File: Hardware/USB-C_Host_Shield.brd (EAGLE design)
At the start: 53.3 x 59.7 mm, 74 parts, among them J1 USB-C, J2 GPIN, J3 GPOUT, U1 ARDUINO_UNO_R3_SHIELDBASIC, U2 LM1117, U3 74HC4050, U5 MAX3421, U6 3.3V/150mA, Y1 12.0mhZ

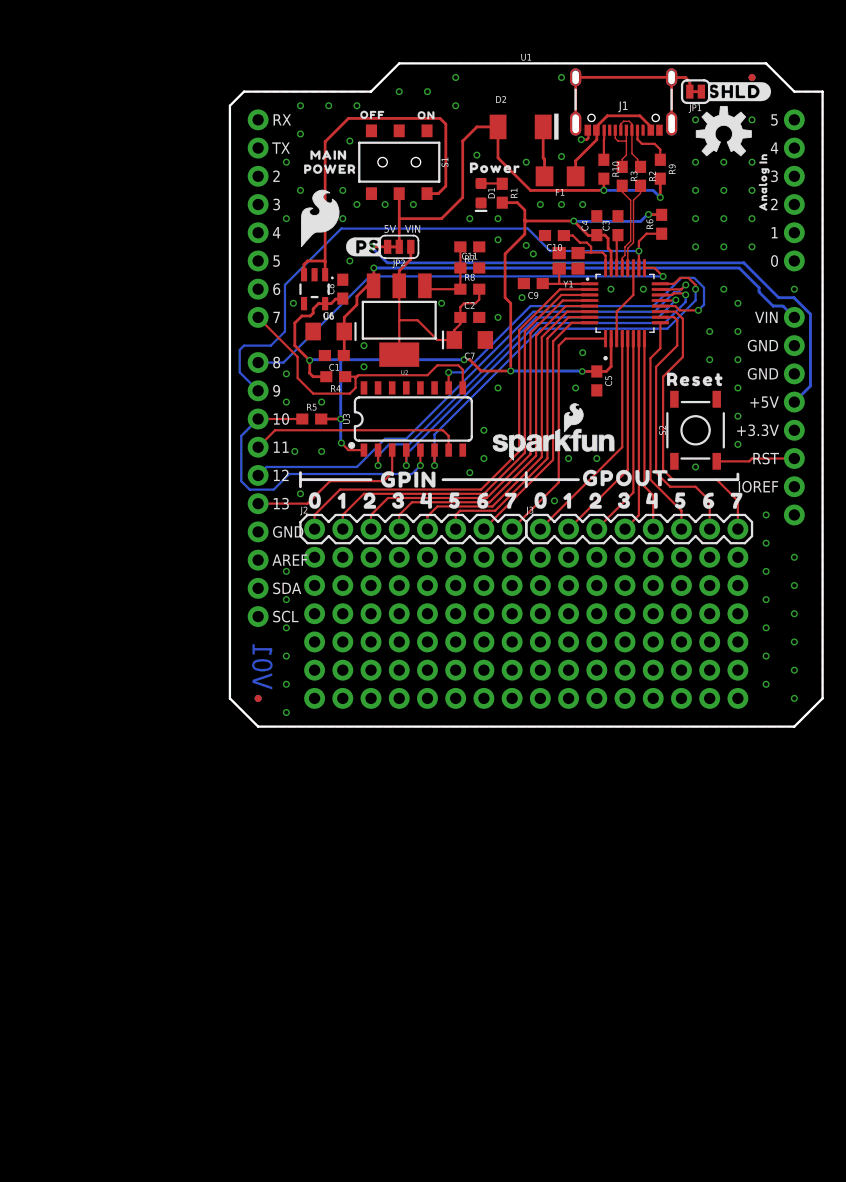
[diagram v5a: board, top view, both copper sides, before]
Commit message: Finalized schematic
Added new switch instead of trace jumper for power switch between VIN and 5V
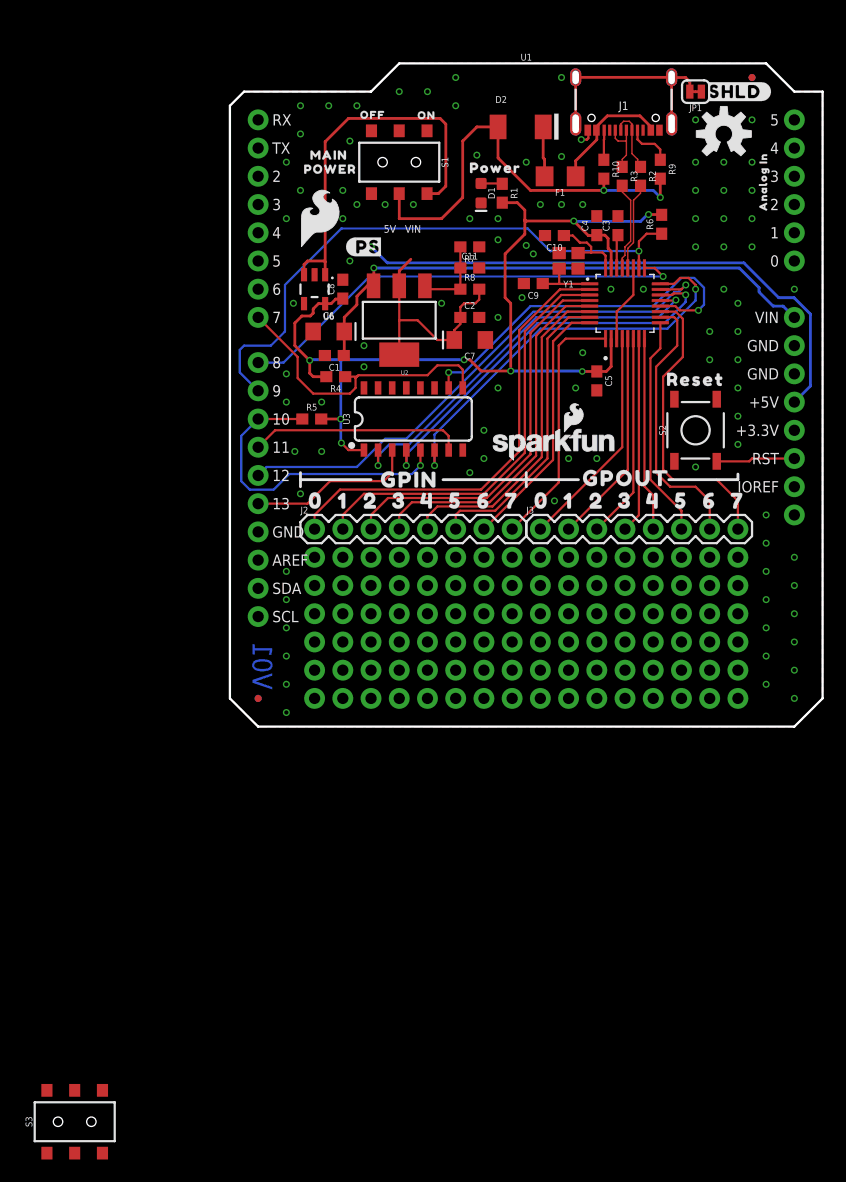
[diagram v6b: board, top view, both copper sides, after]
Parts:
- removed JP2: Power Select, SparkFun-Jumpers:SMT-JUMPER_3_1-NC_TRACE_SILK
- added S3: Power Select, SparkFun-Switches:SWITCH_DPDT_SMD_AYZ0202
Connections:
- net 5V: now also S3.3; no longer JP2.3
- net N$6: now also S3.1; no longer JP2.1
- net VDD: now also S3.2; no longer JP2.2
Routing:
- net VDD: track 41.7 -> 39.2 mm
- net 5V: track 52.0 -> 50.5 mm
- net N$6: track 21.9 -> 20.8 mm
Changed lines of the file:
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@@
 <layer number="44" name="Drills" color="7" fill="1" visible="no" active="yes"/>
 <layer number="45" name="Holes" color="7" fill="1" visible="yes" active="yes"/>
-<layer number="46" name="Milling" color="3" fill="1" visible="yes" active="yes"/>
+<layer number="46" name="Milling" color="3" fill="1" visible="no" active="yes"/>
 <layer number="47" name="Measures" color="7" fill="1" visible="no" active="yes"/>
 <layer number="48" name="Document" color="7" fill="1" visible="no" active="yes"/>
@@
 <attribute name="VALUE" x="9.525" y="29.718" size="0.6096" layer="27" font="vector" ratio="20" rot="R180" align="top-center"/>
 </element>
-<element name="JP2" library="SparkFun-Jumpers" package="SMT-JUMPER_3_1-NC_TRACE_SILK" package3d_urn="urn:adsk.eagle:package:39288/1" value="Power Select" x="15.24" y="40.64" smashed="yes" rot="R180">
-<attribute name="NAME" x="15.24" y="39.497" size="0.6096" layer="25" font="vector" ratio="20" rot="R180" align="bottom-center"/>
-<attribute name="VALUE" x="15.24" y="41.783" size="0.6096" layer="27" font="vector" ratio="20" rot="R180" align="top-center"/>
-</element>
 <element name="U$10" library="output" package="#PS7654332156" value="" x="12.446" y="40.64" smashed="yes"/>
 <element name="R5" library="SparkFun-Resistors" package="0603" value="2.2k" x="7.366" y="25.146" smashed="yes">
@@
 <element name="U5" library="SparkFun-IC-Microcontroller" package="TQFP32" value="MAX3421" x="35.56" y="35.56" smashed="yes" rot="R90">
 <attribute name="PROD_ID" value="IC-09517" x="35.56" y="35.56" size="1.778" layer="27" font="vector" ratio="15" rot="R90" display="off"/>
+</element>
+<element name="S3" library="SparkFun-Switches" package="SWITCH_DPDT_SMD_AYZ0202" value="Power Select" x="-13.97" y="-38.1" smashed="yes">
+<attribute name="NAME" x="-17.78" y="-38.1" size="0.6096" layer="25" font="vector" ratio="20" rot="R90" align="bottom-center"/>
+<attribute name="PROD_ID" value="SWCH-08179" x="-13.97" y="-38.1" size="1.778" layer="27" font="vector" ratio="15" display="off"/>
+<attribute name="SF_ID" value="COM-00597" x="-13.97" y="-38.1" size="1.778" layer="27" font="vector" ratio="15" display="off"/>
+<attribute name="VALUE" x="-10.16" y="-38.1" size="0.6096" layer="27" font="vector" ratio="20" rot="R90" align="top-center"/>
 </element>
 </elements>
@@
 <wire x1="52.25" y1="34.583" x2="52.25" y2="28.12" width="0.254" layer="16"/>
 <wire x1="52.25" y1="28.12" x2="50.8" y2="26.67" width="0.254" layer="16"/>
-<contactref element="JP2" pad="3"/>
 <via x="12.725" y="40.64" extent="1-16" drill="0.381"/>
-<wire x1="12.725" y1="40.64" x2="14.1986" y2="40.64" width="0.254" layer="1"/>
+<contactref element="S3" pad="3"/>
+<wire x1="-11.47" y1="-35.275" x2="12.725" y2="40.64" width="0" layer="19" extent="1-1"/>
 </signal>
 <signal name="SCK-IN">
@@
 <wire x1="20.74" y1="33.694" x2="20.74" y2="34.29" width="0.2032" layer="1"/>
 <wire x1="20.19" y1="33.144" x2="20.74" y2="33.694" width="0.2032" layer="1"/>
-<contactref element="JP2" pad="1"/>
-<wire x1="16.2814" y1="39.5224" x2="16.2814" y2="40.64" width="0.254" layer="1"/>
 <wire x1="15.24" y1="38.481" x2="16.2814" y2="39.5224" width="0.254" layer="1"/>
+<contactref element="S3" pad="1"/>
+<wire x1="15.24" y1="30.937" x2="-16.47" y2="-35.275" width="0" layer="19" extent="1-1"/>
 </signal>
 <signal name="N$8">
@@
 <via x="38.735" y="45.085" extent="1-16" drill="0.381"/>
 <wire x1="38.735" y1="46.775" x2="38.735" y2="45.085" width="0.254" layer="1"/>
-<contactref element="JP2" pad="2"/>
 <contactref element="S1" pad="2"/>
-<wire x1="15.24" y1="40.64" x2="15.24" y2="43.18" width="0.254" layer="1"/>
 <wire x1="15.24" y1="43.18" x2="15.24" y2="45.435" width="0.254" layer="1"/>
 <wire x1="19.05" y1="43.18" x2="15.24" y2="43.18" width="0.254" layer="1"/>
@@
 <wire x1="33.655" y1="45.72" x2="38.1" y2="45.72" width="0.254" layer="16"/>
 <wire x1="38.1" y1="45.72" x2="38.735" y2="45.085" width="0.254" layer="16"/>
+<contactref element="S3" pad="2"/>
+<wire x1="-13.97" y1="-35.275" x2="15.24" y2="45.435" width="0" layer="19" extent="1-1"/>
 </signal>
 <signal name="N$5">

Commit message: Updated layout
Completed layout changes from adding new switch and adjusting the silk screen to be buzzard labels
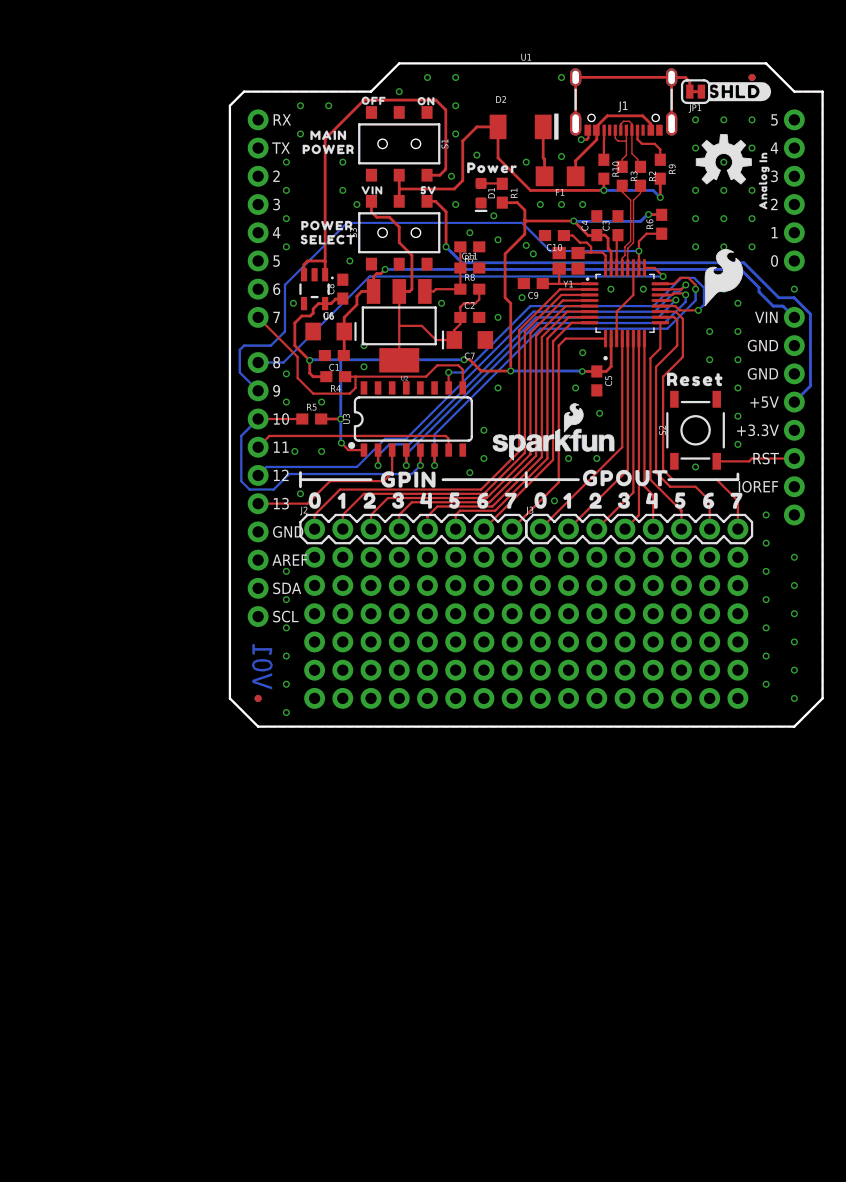
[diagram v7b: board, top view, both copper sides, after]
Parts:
- added U$1: (no value), output:5V6
- added U$12: (no value), output:VIN7
- added U$13: (no value), output:SELECT12
- U$10: device output:#PS7654332156 -> output:POWER11
- moved S3 85.2 mm to (15.2, 41.9)
- moved U$4 36.7 mm to (44.5, 37.8)
- moved U$10 4.15 mm to (8.76, 42.5)
- moved LOGO1 2.54 mm to (44.5, 48.3)
- moved U$14 1.78 mm to (8.89, 49.4)
- moved U$15 1.78 mm to (8.89, 50.7)
- moved S1 1.65 mm to (15.2, 49.9)
- moved U$7 1.28 mm to (13.0, 53.8)
- moved U$5 1.27 mm to (17.7, 53.7)
- moved U2 0.51 mm to (15.2, 33.5)
- moved U$2 0.25 mm to (23.6, 47.8)
- moved U$8 0.13 mm to (48.0, 46.6)
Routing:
- net N$6: track 20.8 -> 29.1 mm
- net VDD: track 39.2 -> 37.3 mm
- net 5V: track 50.5 -> 49.1 mm
- net POWER_IN: track 34.4 -> 35.1 mm
- net PICO: track 19.3 -> 18.7 mm
- net GND: track 8.71 -> 8.41 mm, vias 98 -> 100
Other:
- board text removed: "5V"
- board text removed: "VIN"

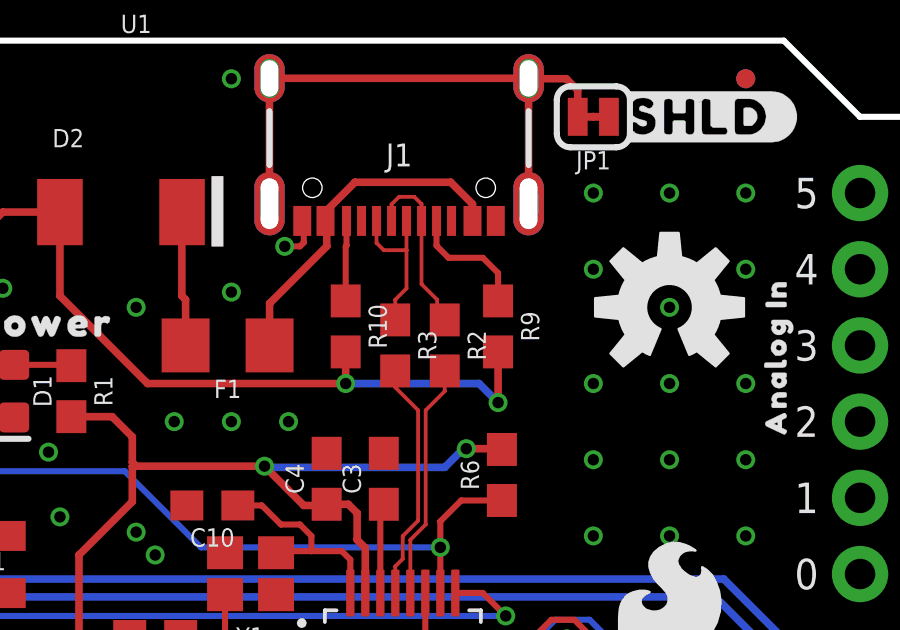
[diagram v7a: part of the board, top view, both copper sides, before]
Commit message: Added product ID to R9 and R10
Created new part in Sparkle for this 56k 0603 resistor that is already input. The new ID, RES-17211, was added to the part and going to be add to the SparkFun parts library after project is verified with components and all
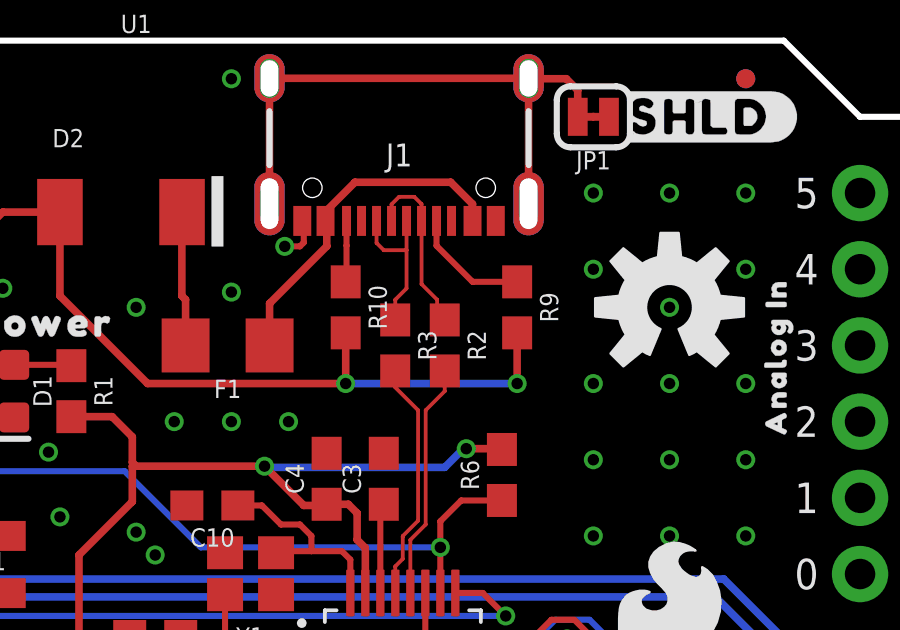
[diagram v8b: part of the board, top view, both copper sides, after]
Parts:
- moved R9 0.90 mm to (39.4, 48.3)
- moved R10 0.63 mm to (33.7, 48.3)
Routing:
- net VDD: track 37.3 -> 38.3 mm
- net CC2: track 2.68 -> 2.04 mm
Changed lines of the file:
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@@
 <drawing>
 <settings>
-<setting alwaysvectorfont="yes"/>
+<setting alwaysvectorfont="no"/>
 <setting verticaltext="up"/>
 </settings>
@@
 <attribute name="VALUE" x="11.43" y="49.911" size="0.6096" layer="27" font="vector" ratio="20" rot="R270" align="top-center"/>
 </element>
-<element name="R9" library="SparkFun-Resistors" package="0603" value="56k" x="38.735" y="47.625" smashed="yes" rot="R270">
-<attribute name="NAME" x="39.497" y="47.625" size="0.6096" layer="25" font="vector" ratio="20" rot="R270" align="bottom-center"/>
-<attribute name="VALUE" x="37.973" y="47.625" size="0.6096" layer="27" font="vector" ratio="20" rot="R270" align="top-center"/>
-</element>
-<element name="R10" library="SparkFun-Resistors" package="0603" value="56k" x="33.655" y="47.625" smashed="yes" rot="R270">
-<attribute name="NAME" x="34.417" y="47.625" size="0.6096" layer="25" font="vector" ratio="20" rot="R270" align="bottom-center"/>
-<attribute name="VALUE" x="32.893" y="47.625" size="0.6096" layer="27" font="vector" ratio="20" rot="R270" align="top-center"/>
-</element>
 <element name="D2" library="SparkFun-DiscreteSemi" package="DO-214BA" value="1A/15V/220mV" x="26.162" y="51.435" smashed="yes">
 <attribute name="NAME" x="23.876" y="53.594" size="0.6096" layer="25" ratio="20"/>
@@
 <element name="U$10" library="output" package="POWER11" value="" x="8.763" y="42.545" smashed="yes"/>
 <element name="U$13" library="output" package="SELECT12" value="" x="8.89" y="41.275" smashed="yes"/>
+<element name="R9" library="SparkFun-Resistors" package="0603" value="56k" x="39.37" y="48.26" smashed="yes" rot="R270">
+<attribute name="NAME" x="40.132" y="48.26" size="0.6096" layer="25" font="vector" ratio="20" rot="R270" align="bottom-center"/>
+<attribute name="PROD_ID" value="RES-17211" x="39.37" y="48.26" size="1.778" layer="27" font="vector" ratio="15" rot="R270" display="off"/>
+<attribute name="VALUE" x="38.608" y="48.26" size="0.6096" layer="27" font="vector" ratio="20" rot="R270" align="top-center"/>
+</element>
+<element name="R10" library="SparkFun-Resistors" package="0603" value="56k" x="33.655" y="48.26" smashed="yes" rot="R270">
+<attribute name="NAME" x="34.417" y="48.26" size="0.6096" layer="25" font="vector" ratio="20" rot="R270" align="bottom-center"/>
+<attribute name="PROD_ID" value="RES-17211" x="33.655" y="48.26" size="1.778" layer="27" font="vector" ratio="15" rot="R270" display="off"/>
+<attribute name="VALUE" x="32.893" y="48.26" size="0.6096" layer="27" font="vector" ratio="20" rot="R270" align="top-center"/>
+</element>
 </elements>
 <signals>
@@
 <signal name="CC1">
 <contactref element="J1" pad="A5"/>
+<wire x1="36.683" y1="51.14" x2="36.683" y2="50.312" width="0.2032" layer="1"/>
 <contactref element="R9" pad="1"/>
-<wire x1="36.683" y1="51.14" x2="36.683" y2="50.312" width="0.2032" layer="1"/>
-<wire x1="36.683" y1="50.312" x2="37.084" y2="49.911" width="0.2032" layer="1"/>
-<wire x1="38.227" y1="49.911" x2="38.735" y2="49.403" width="0.2032" layer="1"/>
-<wire x1="38.735" y1="49.403" x2="38.735" y2="48.475" width="0.2032" layer="1"/>
-<wire x1="37.084" y1="49.911" x2="38.227" y2="49.911" width="0.2032" layer="1"/>
+<wire x1="37.885" y1="49.11" x2="39.37" y2="49.11" width="0.2032" layer="1"/>
+<wire x1="36.683" y1="50.312" x2="37.885" y2="49.11" width="0.2032" layer="1"/>
 </signal>
 <signal name="CC2">
 <contactref element="J1" pad="B5"/>
+<wire x1="33.683" y1="51.14" x2="33.683" y2="50.8" width="0.2032" layer="1"/>
+<wire x1="33.683" y1="50.8" x2="33.683" y2="50.32" width="0.2032" layer="1"/>
 <contactref element="R10" pad="1"/>
-<wire x1="33.683" y1="51.14" x2="33.683" y2="50.32" width="0.2032" layer="1"/>
-<wire x1="33.683" y1="50.32" x2="33.655" y2="50.292" width="0.2032" layer="1"/>
-<wire x1="33.655" y1="50.292" x2="33.655" y2="48.475" width="0.2032" layer="1"/>
+<wire x1="33.683" y1="50.32" x2="33.683" y2="49.138" width="0.2032" layer="1"/>
+<wire x1="33.683" y1="49.138" x2="33.655" y2="49.11" width="0.2032" layer="1"/>
 </signal>
 <signal name="VBUS">
@@
 </signal>
 <signal name="VDD">
-<contactref element="R9" pad="2"/>
-<contactref element="R10" pad="2"/>
 <contactref element="D2" pad="A"/>
 <wire x1="24.13" y1="51.435" x2="22.225" y2="51.435" width="0.254" layer="1"/>
@@
 <via x="33.655" y="45.72" extent="1-16" drill="0.381"/>
 <wire x1="27.051" y1="45.72" x2="33.655" y2="45.72" width="0.254" layer="1"/>
-<via x="38.735" y="45.085" extent="1-16" drill="0.381"/>
-<wire x1="38.735" y1="46.775" x2="38.735" y2="45.085" width="0.254" layer="1"/>
+<via x="39.37" y="45.72" extent="1-16" drill="0.381"/>
 <contactref element="S1" pad="2"/>
 <wire x1="15.24" y1="45.847" x2="15.24" y2="47.086" width="0.254" layer="1"/>
 <wire x1="20.193" y1="45.847" x2="15.24" y2="45.847" width="0.254" layer="1"/>
-<wire x1="33.655" y1="45.72" x2="33.655" y2="46.775" width="0.254" layer="1"/>
-<wire x1="33.655" y1="45.72" x2="38.1" y2="45.72" width="0.254" layer="16"/>
-<wire x1="38.1" y1="45.72" x2="38.735" y2="45.085" width="0.254" layer="16"/>
+<wire x1="33.655" y1="45.72" x2="39.37" y2="45.72" width="0.254" layer="16"/>
 <contactref element="S3" pad="2"/>
 <wire x1="15.24" y1="44.735" x2="15.24" y2="45.847" width="0.254" layer="1"/>
+<contactref element="R9" pad="2"/>
+<contactref element="R10" pad="2"/>
+<wire x1="33.655" y1="45.72" x2="33.655" y2="47.41" width="0.254" layer="1"/>
+<wire x1="39.37" y1="47.41" x2="39.37" y2="45.72" width="0.254" layer="1"/>
 </signal>
 <signal name="N$5">
